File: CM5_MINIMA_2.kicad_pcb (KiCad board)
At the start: 6 copper layers, 54.6 x 57.1 mm, 99 parts, among them J101 USB_C_Receptacle_USB2.0, J501 690-019-298-412, J502 I2C, J503 SPI, J601 JST_SHBM04B-SRSS-TB, J701 Bus_M.2_Socket_M, J802 Conn_01x22_Female, SW602 B3U-3000P, T401 7498111120AR, U401 TPD4EUSB30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

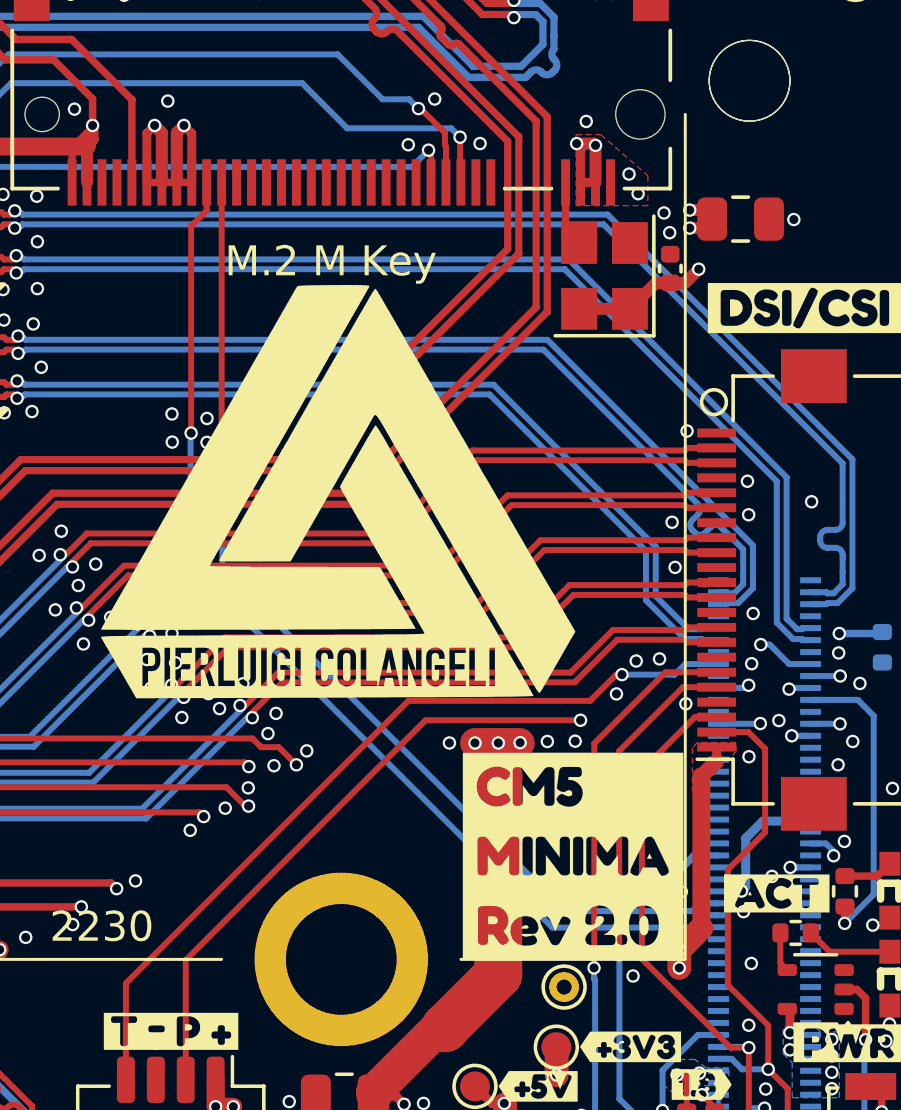
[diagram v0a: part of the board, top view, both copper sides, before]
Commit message: swap TX RX M2
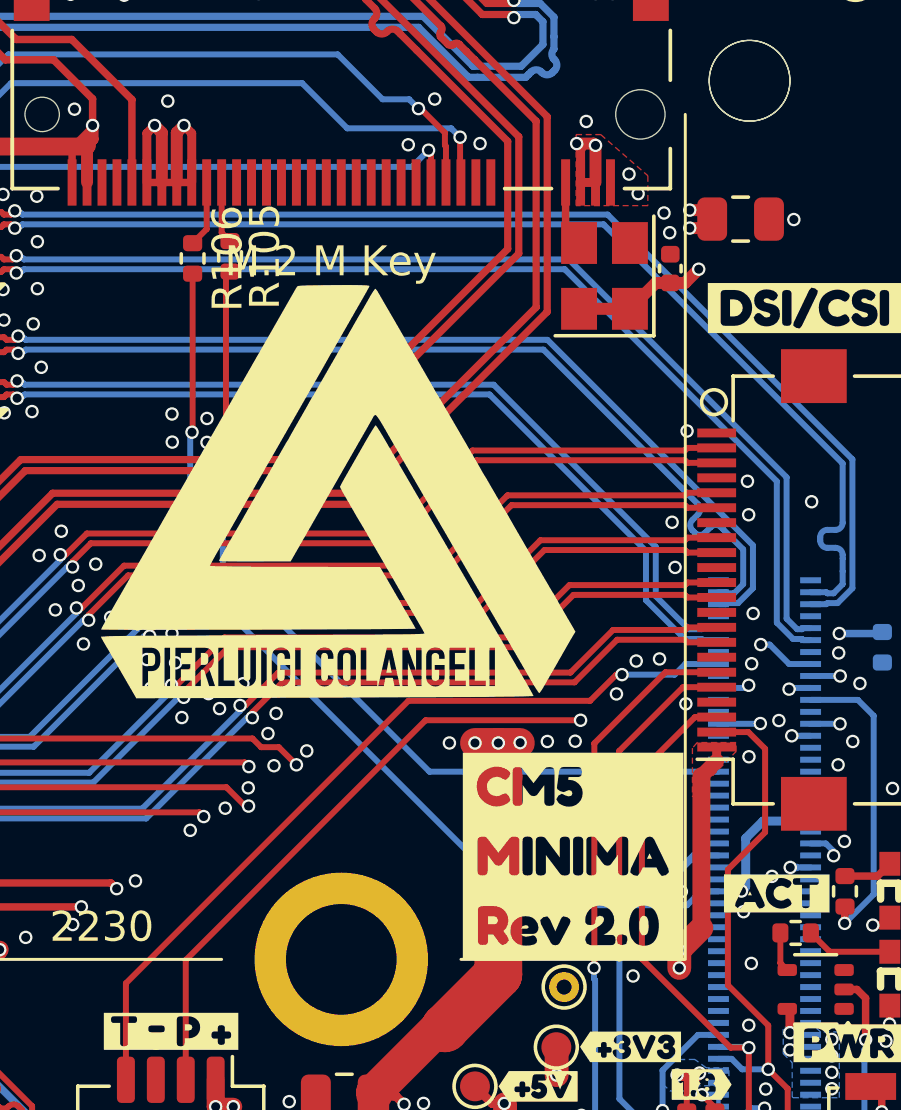
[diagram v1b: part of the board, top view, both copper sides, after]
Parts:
- added R105: 0R, Resistor_SMD:R_0402_1005Metric, F.Cu at (109.9, 35.5)
- added R106: 0R, Resistor_SMD:R_0402_1005Metric, F.Cu at (108.6, 35.5)
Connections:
- J701 pad 20: /CM5/GPIO2 -> /PCIe-M2/TX
- J701 pad 22: /CM5/GPIO3 -> /PCIe-M2/RX
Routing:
- net /CM5/GPIO2: track 35.9 -> 0.00 mm, vias 1 -> 0
- net /CM5/GPIO3: track 34.4 -> 0.00 mm, vias 1 -> 0
- net /CM5/GPIO4: track 0.00 -> 32.5 mm, vias 0 -> 1
- net /CM5/GPIO5: track 0.00 -> 29.3 mm, vias 0 -> 1
- net /PCIe-M2/TX: track 0.00 -> 2.22 mm
- net /PCIe-M2/RX: track 0.00 -> 2.08 mm

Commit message: polish
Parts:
- moved R105 0.54 mm to (109.8, 36.0)
- moved R106 0.53 mm to (108.9, 36.0)
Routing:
- net /CM5/GPIO5: track 29.3 -> 28.6 mm
- net /CM5/GPIO4: track 32.5 -> 32.0 mm
- net /PCIe-M2/RX: track 2.08 -> 2.60 mm
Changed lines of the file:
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@@
 	(footprint "Resistor_SMD:R_0402_1005Metric"
 		(layer "F.Cu")
-		(at 109.88 35.47 -90)
+		(at 109.83 36.01 -90)
 		(descr "Resistor SMD 0402 (1005 Metric), square (rectangular) end terminal, IPC_7351 nominal, (Body size source: IPC-SM-782 page 72, https://www.pcb-3d.com/wordpress/wp-content/uploads/ipc-sm-782a_amendment_1_and_2.pdf), generated with kicad-footprint-generator")
 		(tags "resistor")
@@
 	(footprint "Resistor_SMD:R_0402_1005Metric"
 		(layer "F.Cu")
-		(at 108.63 35.54 -90)
+		(at 108.87 36.01 -90)
 		(descr "Resistor SMD 0402 (1005 Metric), square (rectangular) end terminal, IPC_7351 nominal, (Body size source: IPC-SM-782 page 72, https://www.pcb-3d.com/wordpress/wp-content/uploads/ipc-sm-782a_amendment_1_and_2.pdf), generated with kicad-footprint-generator")
 		(tags "resistor")
@@
 	)
 	(via
-		(at 107.95 41.68)
+		(at 108.305 41.71)
 		(size 0.45)
 		(drill 0.3)
@@
 	)
 	(via
-		(at 110.2 40.73)
+		(at 110.355 40.809415)
 		(size 0.45)
 		(drill 0.3)
@@
 	)
 	(via
-		(at 107.94 40.74)
+		(at 108.325 40.794585)
 		(size 0.45)
 		(drill 0.3)
@@
 	)
 	(via
-		(at 109.11 40.89)
+		(at 109.34 40.82)
 		(size 0.45)
 		(drill 0.3)
@@
 	)
 	(via
-		(at 109.11 41.69)
+		(at 109.32 41.68)
 		(size 0.45)
 		(drill 0.3)
@@
 	)
 	(via
-		(at 110.19 41.66)
+		(at 110.37 41.68)
 		(size 0.45)
 		(drill 0.3)
@@
 	)
 	(segment
-		(start 109.745 36.115)
-		(end 109.88 35.98)
+		(start 109.9 36.59)
+		(end 109.83 36.52)
 		(width 0.2)
 		(layer "F.Cu")
@@
 	)
 	(segment
-		(start 109.64 41.3)
-		(end 109.745 41.195)
-		(width 0.2)
-		(layer "F.Cu")
-		(net 45)
-	)
-	(segment
-		(start 109.745 41.195)
-		(end 109.745 36.115)
+		(start 109.9 41.19)
+		(end 109.9 36.59)
 		(width 0.2)
 		(layer "F.Cu")
@@
 	)
 	(via
-		(at 109.64 41.3)
+		(at 109.9 41.19)
 		(size 0.45)
 		(drill 0.3)
@@
 	)
 	(segment
-		(start 109.64 45.79)
+		(start 109.89 46.04)
 		(end 116.55 52.7)
 		(width 0.2)
@@
 	)
 	(segment
+		(start 109.89 41.2)
+		(end 109.89 46.04)
+		(width 0.2)
+		(layer "B.Cu")
+		(net 45)
+	)
+	(segment
 		(start 116.55 52.7)
 		(end 126.21 52.7)
@@
 	)
 	(segment
-		(start 109.64 41.3)
-		(end 109.64 45.79)
+		(start 109.9 41.19)
+		(end 109.89 41.2)
 		(width 0.2)
 		(layer "B.Cu")
@@
 	)
 	(segment
-		(start 108.63 41.33)
-		(end 108.63 36.05)
+		(start 108.78 36.61)
+		(end 108.87 36.52)
+		(width 0.2)
+		(layer "F.Cu")
+		(net 205)
+	)
+	(segment
+		(start 108.76 41.21)
+		(end 108.78 41.19)
 		(width 0.2)
 		(layer "F.Cu")
@@
 	)
 	(segment
-		(start 108.61 41.35)
-		(end 108.63 41.33)
+		(start 108.78 41.19)
+		(end 108.78 36.61)
 		(width 0.2)
 		(layer "F.Cu")
@@
 	)
 	(via
-		(at 108.61 41.35)
+		(at 108.76 41.21)
 		(size 0.45)
 		(drill 0.3)
@@
 	)
 	(segment
-		(start 125.623468 56.7)
-		(end 126.21 56.7)
-		(width 0.2)
-		(layer "B.Cu")
-		(net 205)
-	)
-	(segment
-		(start 108.61 41.35)
-		(end 108.55 41.41)
+		(start 119.615 57.165)
+		(end 125.158468 57.165)
 		(width 0.2)
 		(layer "B.Cu")
@@
 	)
 	(segment
-		(start 108.55 41.41)
-		(end 108.55 46.1)
+		(start 108.76 41.21)
+		(end 108.76 46.31)
 		(width 0.2)
 		(layer "B.Cu")
@@
 	)
 	(segment
-		(start 119.615 57.165)
-		(end 125.158468 57.165)
+		(start 108.76 46.31)
+		(end 119.615 57.165)
 		(width 0.2)
 		(layer "B.Cu")
@@
 	)
 	(segment
-		(start 108.55 46.1)
-		(end 119.615 57.165)
+		(start 125.623468 56.7)
+		(end 126.21 56.7)
 		(width 0.2)
 		(layer "B.Cu")
@@
 	)
 	(segment
-		(start 109.1 34.56)
+		(start 109.1 35.27)
 		(end 109.1 33)
 		(width 0.2)
@@
 	)
 	(segment
-		(start 108.63 35.03)
-		(end 109.1 34.56)
+		(start 108.87 35.5)
+		(end 109.1 35.27)
 		(width 0.2)
 		(layer "F.Cu")
@@
 	)
 	(segment
-		(start 109.6 33)
-		(end 109.6 34.68)
+		(start 109.6 35.27)
+		(end 109.83 35.5)
 		(width 0.2)
 		(layer "F.Cu")
@@
 	)
 	(segment
-		(start 109.6 34.68)
-		(end 109.88 34.96)
+		(start 109.6 33)
+		(end 109.6 35.27)
 		(width 0.2)
 		(layer "F.Cu")

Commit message: rework for JLC
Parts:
- removed JP101: nRPIBOOT, Jumper:SolderJumper-2_P1.3mm_Bridged_RoundedPad1.0x1.5mm
- removed SW602: B3U-3000P, Button_Switch_SMD:SW_SPST_B3U-3000P
- removed kibuzzard-6772E014: G***, kibuzzard-6772E014
- added SW101: MK-11C04-G013, EasyEDA:SW-SMD_MK-11C04-G013, B.Cu at (130.2, 72.9)
- added SW501: TS-1010A-B, EasyEDA:SW-SMD_TS-1010A-B, F.Cu at (130.6, 66.5)
- added kibuzzard-679BB153: G***, kibuzzard-679BB153, F.Cu at (121.3, 55.5)
- J501: value 690-019-298-412 -> GT-HD001B-CNNG1
- kibuzzard-67795592: moved to B.Cu
- moved kibuzzard-67795592 7.38 mm to (125.2, 69.8), turned to 0 degrees
- moved R105 1.09 mm to (109.8, 37.1)
- moved R106 1.09 mm to (108.9, 37.1)
- moved J502 0.37 mm to (126.4, 72.6)
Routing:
- net /CM5/ETH_PI.TRD0_N: track 33.5 -> 42.5 mm
- net /CM5/ETH_PI.TRD0_P: track 33.5 -> 42.5 mm
- net /CM5/PCIE_PI.RX_P: track 45.1 -> 53.6 mm
- net /CM5/PCIE_PI.RX_N: track 45.2 -> 53.6 mm
- net /CM5/ETH_PI.TRD1_P: track 35.9 -> 42.5 mm
- net /CM5/ETH_PI.TRD1_N: track 36.0 -> 42.6 mm
- net /CM5/nRPIBOOT: track 5.05 -> 10.8 mm, vias 1 -> 2
- net /CM5/PCIE_PI.TX_P: track 47.2 -> 51.2 mm
- net /CM5/PCIE_PI.TX_N: track 47.7 -> 51.2 mm
- net /CM5/ETH_PI.TRD2_N: track 40.2 -> 42.9 mm
- net /CM5/ETH_PI.TRD2_P: track 40.2 -> 42.9 mm
- net /USB_C.D_N: track 25.3 -> 24.1 mm
- net /PCIe-M2/TX: track 2.60 -> 3.69 mm
- net /CM5/GPIO4: track 32.0 -> 30.9 mm
- net /PCIe-M2/RX: track 2.60 -> 3.68 mm
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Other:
- board text removed: "0"
- board text removed: "0 mm"
- board text removed: "0.0000 mm / 0.0000 mm"
- board text removed: "0.01 mm"
- board text removed: "0.02"
- board text removed: "0.035 mm"
- board text removed: "0.0525 mm"
- board text removed: "0.13 mm"
- board text removed: "0.3000 mm"
- board text removed: "0.43 mm"
- board text removed: "1"
- board text removed: "1.5150 mm"
- board text removed: "2116 RC58%"
- board text removed: "3.3"
- board text removed: "4.45"
- board text removed: "4.6"
- board text removed: "54.5516 mm x 57.1400 mm"
- board text removed: "6"
- board text removed: "B.Cu"
- board text removed: "B.Mask"
- board text removed: "B.Paste"
- board text removed: "B.Silkscreen"
- board text removed: "BOARD CHARACTERISTICS"
- board text removed: "Board Thickness:"
- board text removed: "Board overall dimensions:"
- board text removed: "Bottom Silk Screen"
- board text removed: "Bottom Solder Mask"
- board text removed: "Bottom Solder Paste"
- board text removed: "Castellated pads:"
- board text removed: "Color"
- board text removed: "Copper Finish:"
- board text removed: "Copper Layer Count:"
- board text removed: "Dielectric"
- board text removed: "ENIG"
- board text removed: "Edge card connectors:"
- board text removed: "Epsilon R"
- board text removed: "F.Cu"
- board text removed: "F.Mask"
- board text removed: "F.Paste"
- board text removed: "F.Silkscreen"
- board text removed: "FR4"
- board text removed: "FR4 natural"
- board text removed: "Impedance Control:"
- board text removed: "In1.Cu"
- board text removed: "In2.Cu"
- board text removed: "In3.Cu"
- board text removed: "In4.Cu"
- board text removed: "Layer Name"
- board text removed: "Loss Tangent"
- board text removed: "Material"
- board text removed: "Min hole diameter:"
- board text removed: "Min track/spacing:"
- board text removed: "No"
- board text removed: "Not specified"
- board text removed: "Plated Board Edge:"
- board text removed: "Thickness (mm)"
- board text removed: "Top Silk Screen"
- board text removed: "Top Solder Mask"
- board text removed: "Top Solder Paste"
- board text removed: "Type"
- board text removed: "Yes"
- board text removed: "copper"
- board text removed: "core"
- board text removed: "prepreg"

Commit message: prod
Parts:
- R501, R502: value 10k -> 2k2
- R605, R606: value 3k3 -> 2k2
- R707: value 1k -> 2k2
- moved kibuzzard-675DA850 1.92 mm to (100.6, 64.1)
- moved kibuzzard-675DA866 0.20 mm to (107.9, 67.6)
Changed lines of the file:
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@@
 			)
 		)
-		(property "Value" "3k3"
+		(property "Value" "2k2"
 			(at 0 1.17 90)
 			(layer "F.Fab")
@@
 	(footprint "kibuzzard-675DA866"
 		(layer "F.Cu")
-		(at 107.9 67.37)
+		(at 107.89 67.57)
 		(descr "Generated with KiBuzzard")
 		(tags "kb_params=eyJBbGlnbm1lbnRDaG9pY2UiOiAiQ2VudGVyIiwgIkNhcExlZnRDaG9pY2UiOiAiWyIsICJDYXBSaWdodENob2ljZSI6ICJdIiwgIkZvbnRDb21ib0JveCI6ICJGcmVkZHlTcGFyay1SZWd1bGFyIiwgIkhlaWdodEN0cmwiOiAxLjIsICJMYXllckNvbWJvQm94IjogIkYuU2lsa1MiLCAiTGluZVNwYWNpbmdDdHJsIjogMS41LCAiTXVsdGlMaW5lVGV4dCI6ICJGQU4iLCAiUGFkZGluZ0JvdHRvbUN0cmwiOiAyLjAsICJQYWRkaW5nTGVmdEN0cmwiOiAzLjAsICJQYWRkaW5nUmlnaHRDdHJsIjogMy4wLCAiUGFkZGluZ1RvcEN0cmwiOiAyLjAsICJXaWR0aEN0cmwiOiAwLjAsICJhZHZhbmNlZENoZWNrYm94IjogZmFsc2UsICJpbmxpbmVGb3JtYXRUZXh0Ym94IjogZmFsc2UsICJsaW5lb3ZlclN0eWxlQ2hvaWNlIjogIlNxdWFyZSIsICJsaW5lb3ZlclRoaWNrbmVzc0N0cmwiOiAxfQ==")
@@
 		(sheetname "Root")
 		(sheetfile "CM5_MINIMA_2.kicad_sch")
-		(attr exclude_from_pos_files)
+		(attr exclude_from_pos_files exclude_from_bom)
 		(fp_circle
 			(center 0 0)
@@
 			)
 		)
-		(property "Value" "1k"
+		(property "Value" "2k2"
 			(at 0 1.17 90)
 			(layer "F.Fab")
@@
 		(sheetname "IO")
 		(sheetfile "IO.kicad_sch")
-		(attr smd exclude_from_pos_files)
+		(attr smd exclude_from_pos_files exclude_from_bom)
 		(fp_line
 			(start -4.04 -1.21)
@@
 	(footprint "kibuzzard-675DA850"
 		(layer "F.Cu")
-		(at 99.099718 65.358528)
+		(at 100.57 64.13)
 		(descr "Generated with KiBuzzard")
 		(tags "kb_params=eyJBbGlnbm1lbnRDaG9pY2UiOiAiQ2VudGVyIiwgIkNhcExlZnRDaG9pY2UiOiAiWyIsICJDYXBSaWdodENob2ljZSI6ICJdIiwgIkZvbnRDb21ib0JveCI6ICJGcmVkZHlTcGFyay1SZWd1bGFyIiwgIkhlaWdodEN0cmwiOiAxLjIsICJMYXllckNvbWJvQm94IjogIkYuU2lsa1MiLCAiTGluZVNwYWNpbmdDdHJsIjogMS41LCAiTXVsdGlMaW5lVGV4dCI6ICJIRE1JIiwgIlBhZGRpbmdCb3R0b21DdHJsIjogMi4wLCAiUGFkZGluZ0xlZnRDdHJsIjogMy4wLCAiUGFkZGluZ1JpZ2h0Q3RybCI6IDMuMCwgIlBhZGRpbmdUb3BDdHJsIjogMi4wLCAiV2lkdGhDdHJsIjogMC4wLCAiYWR2YW5jZWRDaGVja2JveCI6IGZhbHNlLCAiaW5saW5lRm9ybWF0VGV4dGJveCI6IGZhbHNlLCAibGluZW92ZXJTdHlsZUNob2ljZSI6ICJTcXVhcmUiLCAibGluZW92ZXJUaGlja25lc3NDdHJsIjogMX0=")
@@
 			)
 		)
-		(property "Value" "10k"
+		(property "Value" "2k2"
 			(at 0 1.17 0)
 			(layer "F.Fab")
@@
 		(sheetname "Ethernet")
 		(sheetfile "Ethernet.kicad_sch")
-		(attr smd exclude_from_pos_files)
+		(attr smd exclude_from_pos_files exclude_from_bom)
 		(fp_line
 			(start 7.925 -18.31)
@@
 		(sheetname "Root")
 		(sheetfile "CM5_MINIMA_2.kicad_sch")
-		(attr exclude_from_pos_files)
+		(attr exclude_from_pos_files exclude_from_bom)
 		(fp_circle
 			(center 0 0)
@@
 		(sheetname "Root")
 		(sheetfile "CM5_MINIMA_2.kicad_sch")
-		(attr exclude_from_pos_files)
+		(attr exclude_from_pos_files exclude_from_bom)
 		(fp_circle
 			(center 0 0)
@@
 		(sheetname "Root")
 		(sheetfile "CM5_MINIMA_2.kicad_sch")
-		(attr exclude_from_pos_files)
+		(attr exclude_from_pos_files exclude_from_bom)
 		(fp_circle
 			(center 0 0)
@@
 			)
 		)
-		(property "Value" "10k"
+		(property "Value" "2k2"
 			(at 0 1.17 0)
 			(layer "F.Fab")
@@
 			)
 		)
-		(property "Value" "3k3"
+		(property "Value" "2k2"
 			(at 0 1.17 0)
 			(layer "F.Fab")
